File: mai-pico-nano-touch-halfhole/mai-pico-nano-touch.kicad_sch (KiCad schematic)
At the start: 5 parts, among them J1 Conn_01x04, J2 Conn_01x34, U1 MPR121-Module, U2 MPR121-Module, U3 MPR121-Module

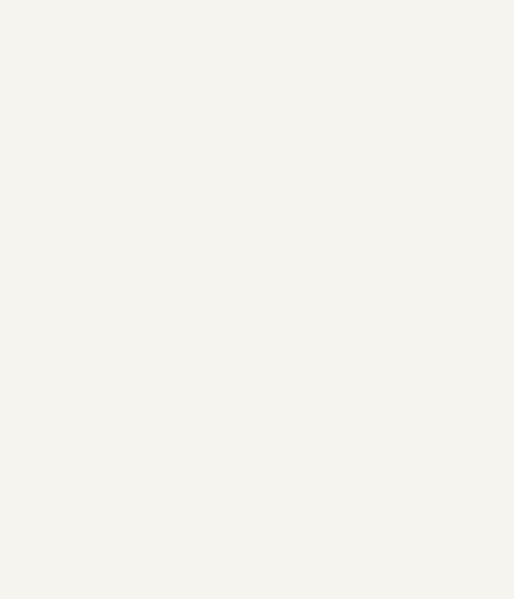
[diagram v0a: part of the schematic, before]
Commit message: Half Hole version mounting holes
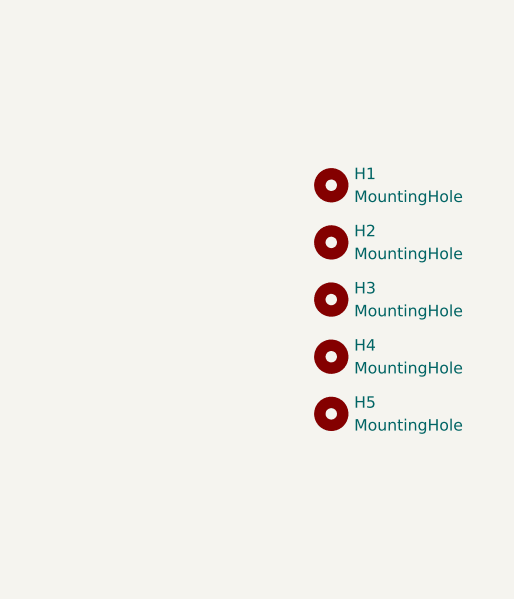
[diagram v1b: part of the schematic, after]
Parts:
- added H1, H2, H3, H4, H5: MountingHole, MountingHole:MountingHole_2.2mm_M2, symbol Mechanical:MountingHole
